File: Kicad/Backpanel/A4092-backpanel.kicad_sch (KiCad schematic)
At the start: 2 parts, among them J1 Conn_02x25_Odd_Even, J2 5787170-5

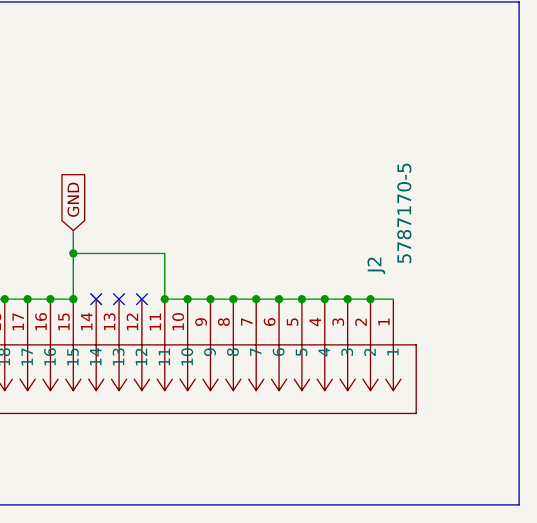
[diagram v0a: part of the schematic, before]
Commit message: Update Backpanel
- Fix part numbers and orientation
- Shift IDC50 connector up to get out of the way of the Zorro
  daughterboard and align better with the 4092 connector
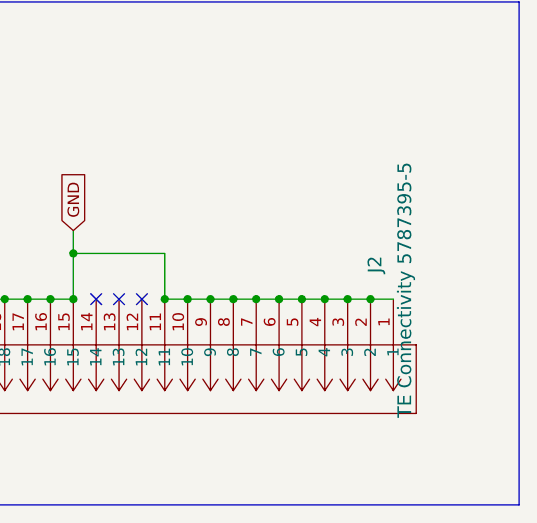
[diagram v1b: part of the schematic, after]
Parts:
- J1: FT Rotation Offset  (none) -> 270; LCSC Part # (none) -> C221059
- J2: value 5787170-5 -> TE Connectivity 5787395-5; FT Rotation Offset (none) -> 90; LCSC Part # (none) -> C3138281
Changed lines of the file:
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@@
 			)
 		)
-		(property "Value" "5787170-5"
+		(property "Value" "TE Connectivity 5787395-5"
 			(at 215.9 109.22 0)
 			(effects
@@
 		)
 		(property "Description" ""
+			(at 214.63 124.46 0)
+			(effects
+				(font
+					(size 1.27 1.27)
+				)
+				(hide yes)
+			)
+		)
+		(property "LCSC Part #" "C3138281"
+			(at 214.63 124.46 0)
+			(effects
+				(font
+					(size 1.27 1.27)
+				)
+				(hide yes)
+			)
+		)
+		(property "FT Rotation Offset" "90"
 			(at 214.63 124.46 0)
 			(effects
@@
 			(effects
 				(font
+					(size 1.27 1.27)
+				)
+				(hide yes)
+			)
+		)
+		(property "LCSC Part #" "C221059"
+			(at 153.67 48.26 90)
+			(effects
+				(font
+					(size 1.27 1.27)
+				)
+				(hide yes)
+			)
+		)
+		(property "FT Rotation Offset " "270"
+			(at 153.67 48.26 90)
+			(effects
+				(font
